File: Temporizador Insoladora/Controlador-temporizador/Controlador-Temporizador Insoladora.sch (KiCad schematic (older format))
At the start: 78 parts, among them P1 ICSP, P10 CONN_01X08, P2 VAC12V, P3 CARGA, P4 TRANSF, P5 VAC, P6 OPTO, P7 CONN_02X08, P8 OPTO, P9 OPTO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

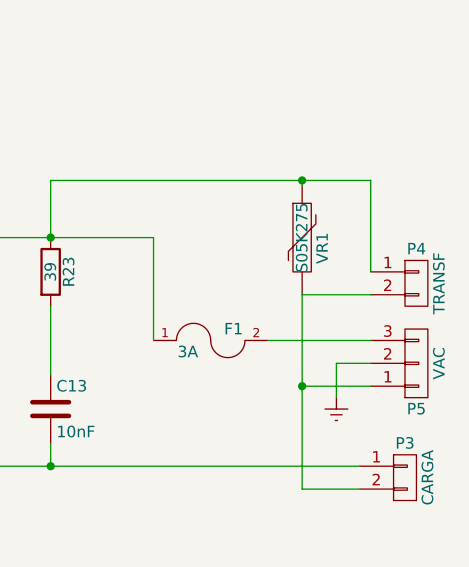
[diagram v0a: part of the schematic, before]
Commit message: Cambiado tamaño de footprint del capacitor y varistor de la parte de potencia
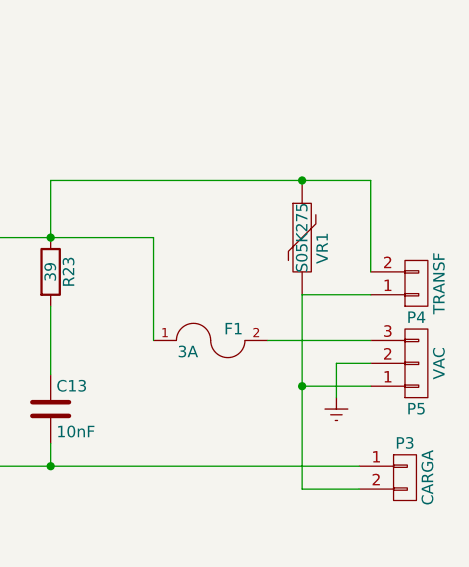
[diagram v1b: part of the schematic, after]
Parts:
- C13: footprint Capacitors_ThroughHole:C_Rect_L7_W2.5_P5 -> Capacitors_ThroughHole:C_Rect_L13_W4_P10
- VR1: footprint Discret:C2 -> Capacitors_ThroughHole:C_Rect_L13_W4_P10
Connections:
- net at F1.1, R18.1, R23.1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: now also P4.2 (P2); no longer P4.1 (P1)
- net at P3.2 (P2), P5.1 (P1), VR1.2: now also P4.1 (P1); no longer P4.2 (P2)
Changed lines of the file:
@@
 F 0 "C13" H 12825 3250 50  0000 L CNN
 F 1 "10nF" H 12825 3050 50  0000 L CNN
-F 2 "Capacitors_ThroughHole:C_Rect_L7_W2.5_P5" H 12838 3000 30  0001 C CNN
+F 2 "Capacitors_ThroughHole:C_Rect_L13_W4_P10" H 12838 3000 30  0001 C CNN
 F 3 "" H 12800 3150 60  0000 C CNN
 	1    12800 3150
@@
 F 3 "" H 14400 2600 60  0000 C CNN
 	1    14400 2600
-	1    0    0    -1
+	1    0    0    1
 $EndComp
 $Comp
@@
 F 0 "VR1" V 13960 2354 50  0000 C TNN
 F 1 "S05K275" V 13900 2400 50  0000 C CNN
-F 2 "Discret:C2" H 13900 2400 60  0001 C CNN
+F 2 "Capacitors_ThroughHole:C_Rect_L13_W4_P10" H 13900 2400 60  0001 C CNN
 F 3 "" H 13900 2400 60  0000 C CNN
 	1    13900 2400

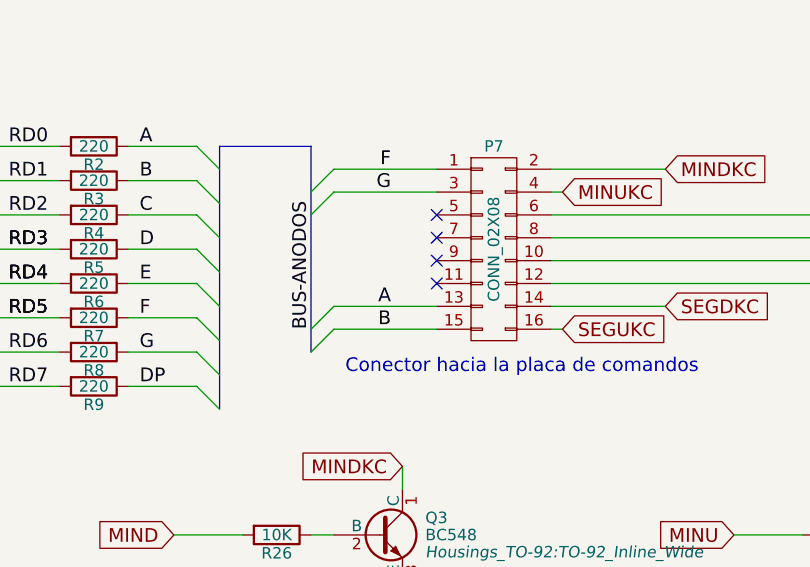
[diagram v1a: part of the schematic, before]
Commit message: Acomodando las referencias de los compònentes para el top silk
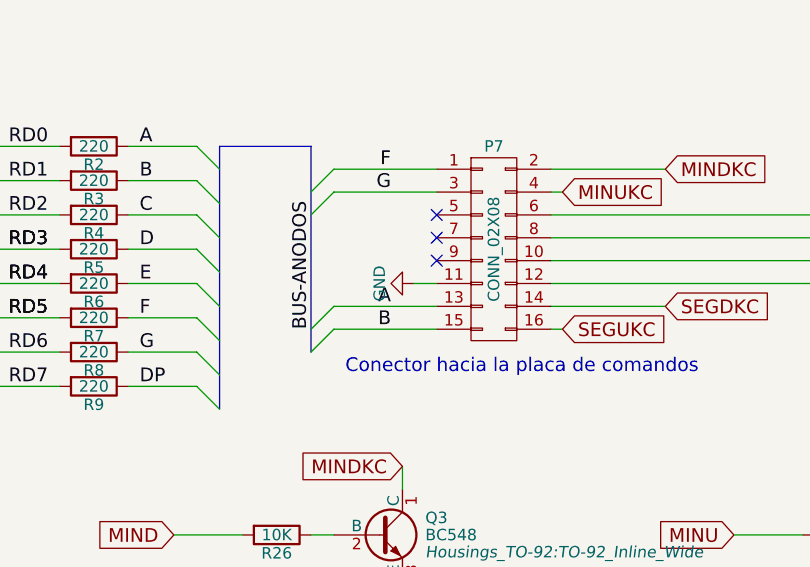
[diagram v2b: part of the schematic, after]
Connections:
- net GND: now also P7.11 (P11)
- no-connect marks 29 -> 28
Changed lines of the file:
@@
 NoConn ~ 4150 8750
 NoConn ~ 4150 8850
-NoConn ~ 4150 8950
 Entry Wire Line
 	3600 8550 3700 8450
@@
 Wire Wire Line
 	8150 6950 8150 7200
+$Comp
+L GND #PWR042
+U 1 1 555F6435
+P 4050 8950
+F 0 "#PWR042" H 4050 8700 50  0001 C CNN
+F 1 "GND" H 4050 8800 50  0000 C CNN
+F 2 "" H 4050 8950 60  0000 C CNN
+F 3 "" H 4050 8950 60  0000 C CNN
+	1    4050 8950
+	0    1    1    0
+$EndComp
+Wire Wire Line
+	4050 8950 4150 8950
 $EndSCHEMATC

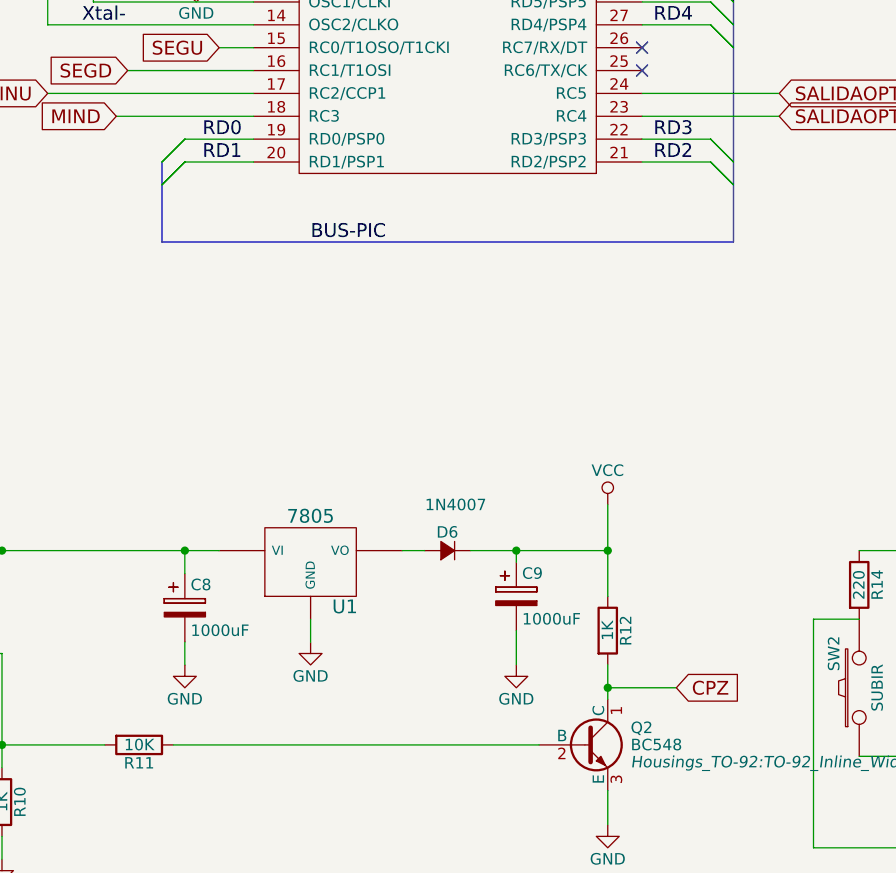
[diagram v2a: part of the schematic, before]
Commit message: Quitando los puentes innecesarios del pcb. Cambio del lugar del diodo de entrada para hacer compatible con el ICSP
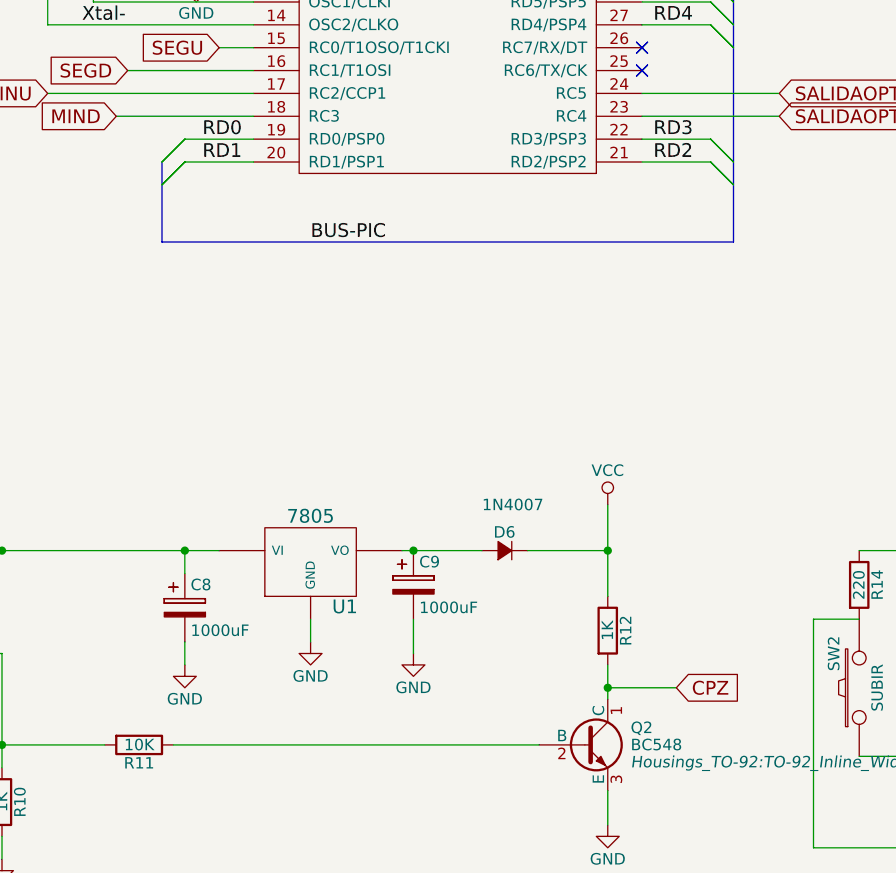
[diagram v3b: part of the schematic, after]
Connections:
- net VCC: no longer C9.1
- net at D6.1 (A), U1.VO: now also C9.1
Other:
- moved on the sheet: C9, D6
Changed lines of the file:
@@
 L CP C9
 U 1 1 552AAAAD
-P 5100 5850
-F 0 "C9" H 5125 5950 50  0000 L CNN
-F 1 "1000uF" H 5125 5750 50  0000 L CNN
-F 2 "Capacitors_ThroughHole:C_Radial_D10_L16_P5" H 5138 5700 30  0001 C CNN
-F 3 "" H 5100 5850 60  0000 C CNN
-	1    5100 5850
+P 4650 5800
+F 0 "C9" H 4675 5900 50  0000 L CNN
+F 1 "1000uF" H 4675 5700 50  0000 L CNN
+F 2 "Capacitors_ThroughHole:C_Radial_D10_L16_P5" H 4688 5650 30  0001 C CNN
+F 3 "" H 4650 5800 60  0000 C CNN
+	1    4650 5800
 	1    0    0    -1
 $EndComp
@@
 L GND #PWR016
 U 1 1 552AAB01
-P 5100 6150
-F 0 "#PWR016" H 5100 5900 50  0001 C CNN
-F 1 "GND" H 5100 6000 50  0000 C CNN
-F 2 "" H 5100 6150 60  0000 C CNN
-F 3 "" H 5100 6150 60  0000 C CNN
-	1    5100 6150
+P 4650 6100
+F 0 "#PWR016" H 4650 5850 50  0001 C CNN
+F 1 "GND" H 4650 5950 50  0000 C CNN
+F 2 "" H 4650 6100 60  0000 C CNN
+F 3 "" H 4650 6100 60  0000 C CNN
+	1    4650 6100
 	1    0    0    -1
 $EndComp
@@
 	5500 5450 5500 5850
 Wire Wire Line
-	5100 6000 5100 6150
-Wire Wire Line
-	5100 5700 5100 5650
-Connection ~ 5100 5650
+	4650 5950 4650 6100
+Connection ~ 4650 5650
 Wire Wire Line
 	3600 6500 5200 6500
@@
 	6050 3150 6050 4300
 Wire Bus Line
-	6050 4300 3550 4300
+	3550 4300 6050 4300
 Wire Bus Line
-	3550 4300 3550 3950
+	3550 3950 3550 4300
 Connection ~ 3650 5650
 Wire Wire Line
@@
 L D_Small D6
 U 1 1 555AB148
-P 4800 5650
-F 0 "D6" H 4750 5730 50  0000 L CNN
-F 1 "1N4007" H 4700 5850 50  0000 L CNN
-F 2 "Diodes_ThroughHole:Diode_DO-41_SOD81_Horizontal_RM10" V 4800 5650 60  0001 C CNN
-F 3 "" V 4800 5650 60  0000 C CNN
-	1    4800 5650
+P 5050 5650
+F 0 "D6" H 5000 5730 50  0000 L CNN
+F 1 "1N4007" H 4950 5850 50  0000 L CNN
+F 2 "Diodes_ThroughHole:Diode_DO-41_SOD81_Horizontal_RM10" V 5050 5650 60  0001 C CNN
+F 3 "" V 5050 5650 60  0000 C CNN
+	1    5050 5650
 	1    0    0    -1
 $EndComp
 Connection ~ 5500 5650
 Wire Wire Line
-	4600 5650 4700 5650
-Wire Wire Line
-	4900 5650 5500 5650
+	4600 5650 4950 5650
+Wire Wire Line
+	5150 5650 5500 5650
 Wire Wire Line
 	1100 4600 1100 4700

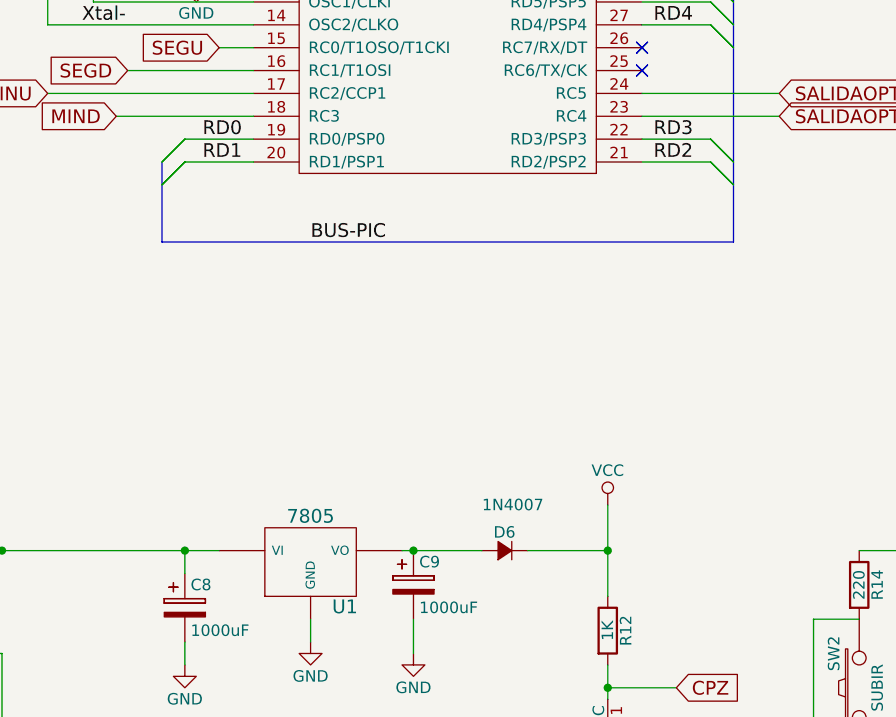
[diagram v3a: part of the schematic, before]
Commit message: Agrandado de pads en footprint de algunos componentes
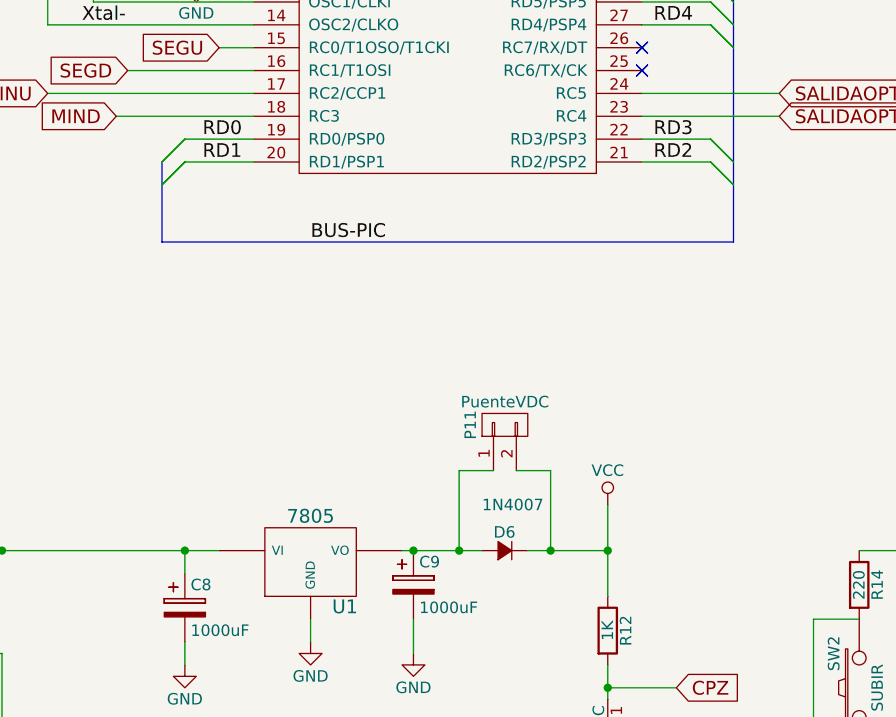
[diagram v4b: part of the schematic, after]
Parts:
- added P11: PuenteVDC, Socket_Strips:Socket_Strip_Straight_1x02, symbol CONN_01X02
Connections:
- net VCC: now also P11.2 (P2)
- net at C9.1, D6.1 (A), U1.VO: now also P11.1 (P1)
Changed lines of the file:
@@
 	6050 3150 6050 4300
 Wire Bus Line
-	3550 4300 6050 4300
+	6050 4300 3550 4300
 Wire Bus Line
-	3550 3950 3550 4300
+	3550 4300 3550 3950
 Connection ~ 3650 5650
 Wire Wire Line
@@
 Wire Wire Line
 	4050 8950 4150 8950
+$Comp
+L CONN_01X02 P11
+U 1 1 5560B911
+P 5050 5100
+F 0 "P11" H 5050 5250 50  0000 C CNN
+F 1 "PuenteVDC" V 5150 5100 50  0000 C CNN
+F 2 "Socket_Strips:Socket_Strip_Straight_1x02" H 5050 5100 60  0001 C CNN
+F 3 "" H 5050 5100 60  0000 C CNN
+	1    5050 5100
+	0    -1   -1   0
+$EndComp
+Wire Wire Line
+	5100 5300 5250 5300
+Wire Wire Line
+	5250 5300 5250 5650
+Connection ~ 5250 5650
+Wire Wire Line
+	5000 5300 4850 5300
+Wire Wire Line
+	4850 5300 4850 5650
+Connection ~ 4850 5650
 $EndSCHEMATC

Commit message: Cambiado footprint del triac controlador. Placa controlador teminada. Placa Comandos terminada
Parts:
- U4: footprint Discret:TO220 -> Transistors_TO-220:TO-220_Neutral123_Horizontal_LargePads
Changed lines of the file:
@@
 F 0 "U4" H 12000 3150 50  0000 C CNN
 F 1 "TRIAC" H 11950 2550 50  0000 C CNN
-F 2 "Discret:TO220" H 12250 2800 60  0001 C CNN
+F 2 "Transistors_TO-220:TO-220_Neutral123_Horizontal_LargePads" H 12250 2800 60  0001 C CNN
 F 3 "" H 12250 2800 60  0000 C CNN
 	1    12250 2800
